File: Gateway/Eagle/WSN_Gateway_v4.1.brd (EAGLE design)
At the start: 98.7 x 27.9 mm, 17 parts, among them J1 5.5x2.1mm Barrel

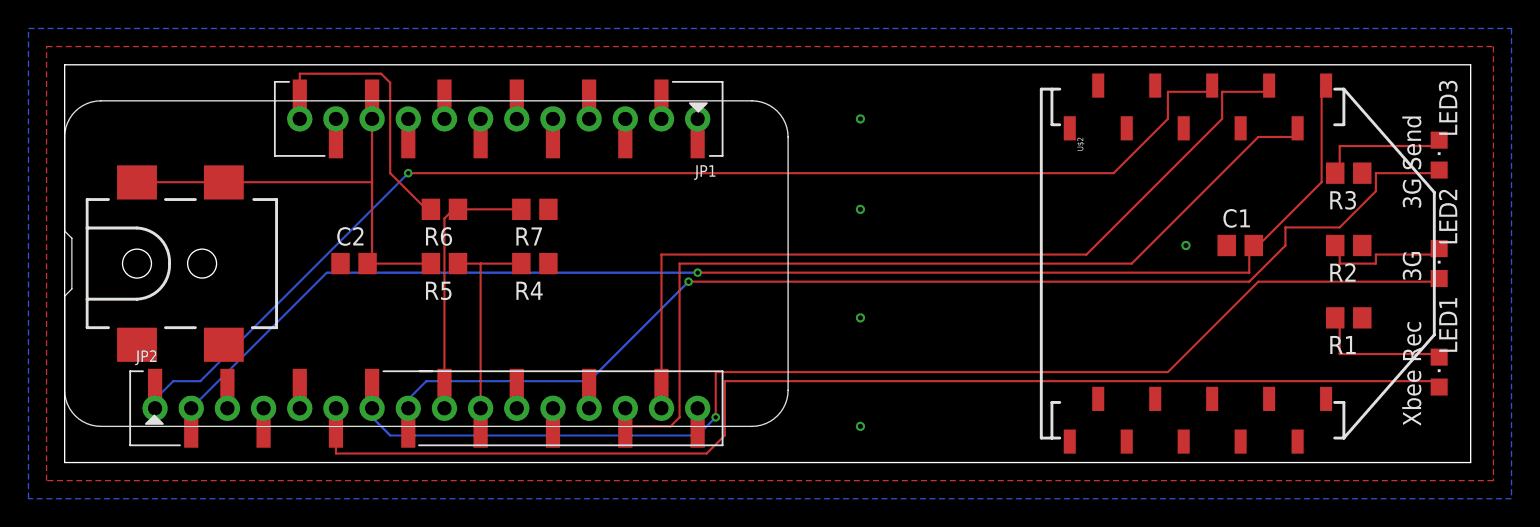
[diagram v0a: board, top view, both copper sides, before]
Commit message: Added new Gateway versions (with improved integrety against signal interference)
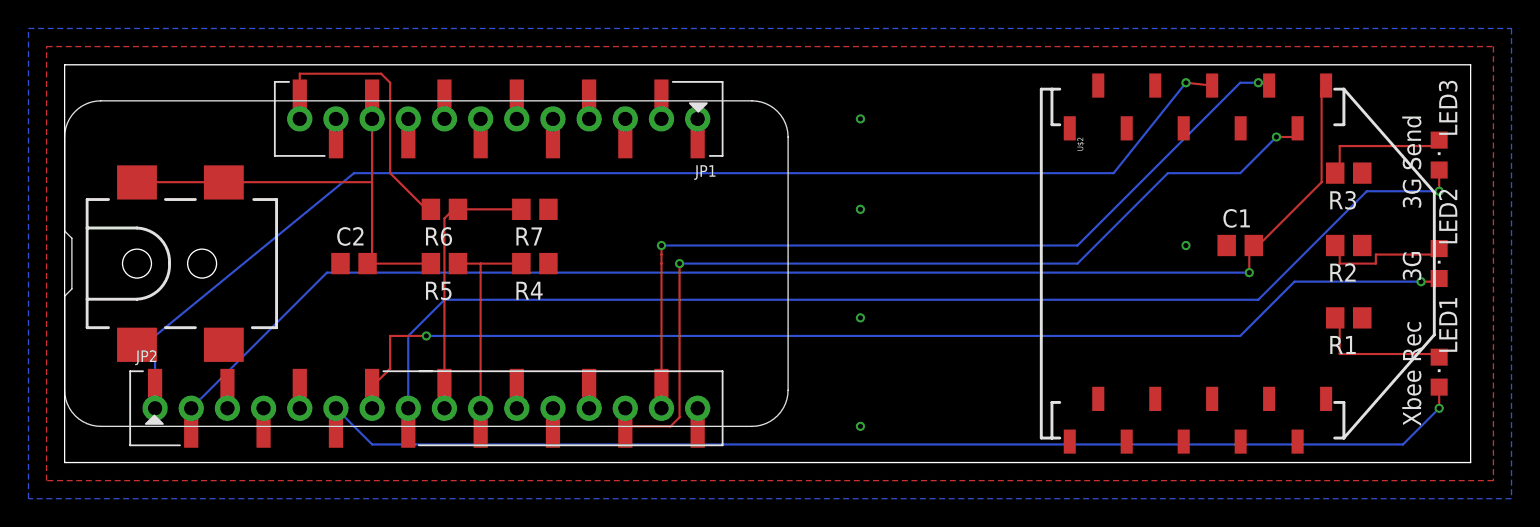
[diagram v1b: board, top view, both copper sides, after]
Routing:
- net LED2: track 84.2 -> 80.9 mm, vias 1 -> 2
- net LED1: track 85.4 -> 83.0 mm, vias 0 -> 1
- net LED3: track 82.8 -> 84.5 mm
- net RESET: track 86.9 -> 88.4 mm
- net XBEE_RX: track 59.6 -> 59.3 mm, vias 0 -> 2
- net XBEE_TX: vias 0 -> 2
